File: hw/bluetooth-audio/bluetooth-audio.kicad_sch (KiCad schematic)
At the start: 1 part, among them U1 STM32WB55CGUx

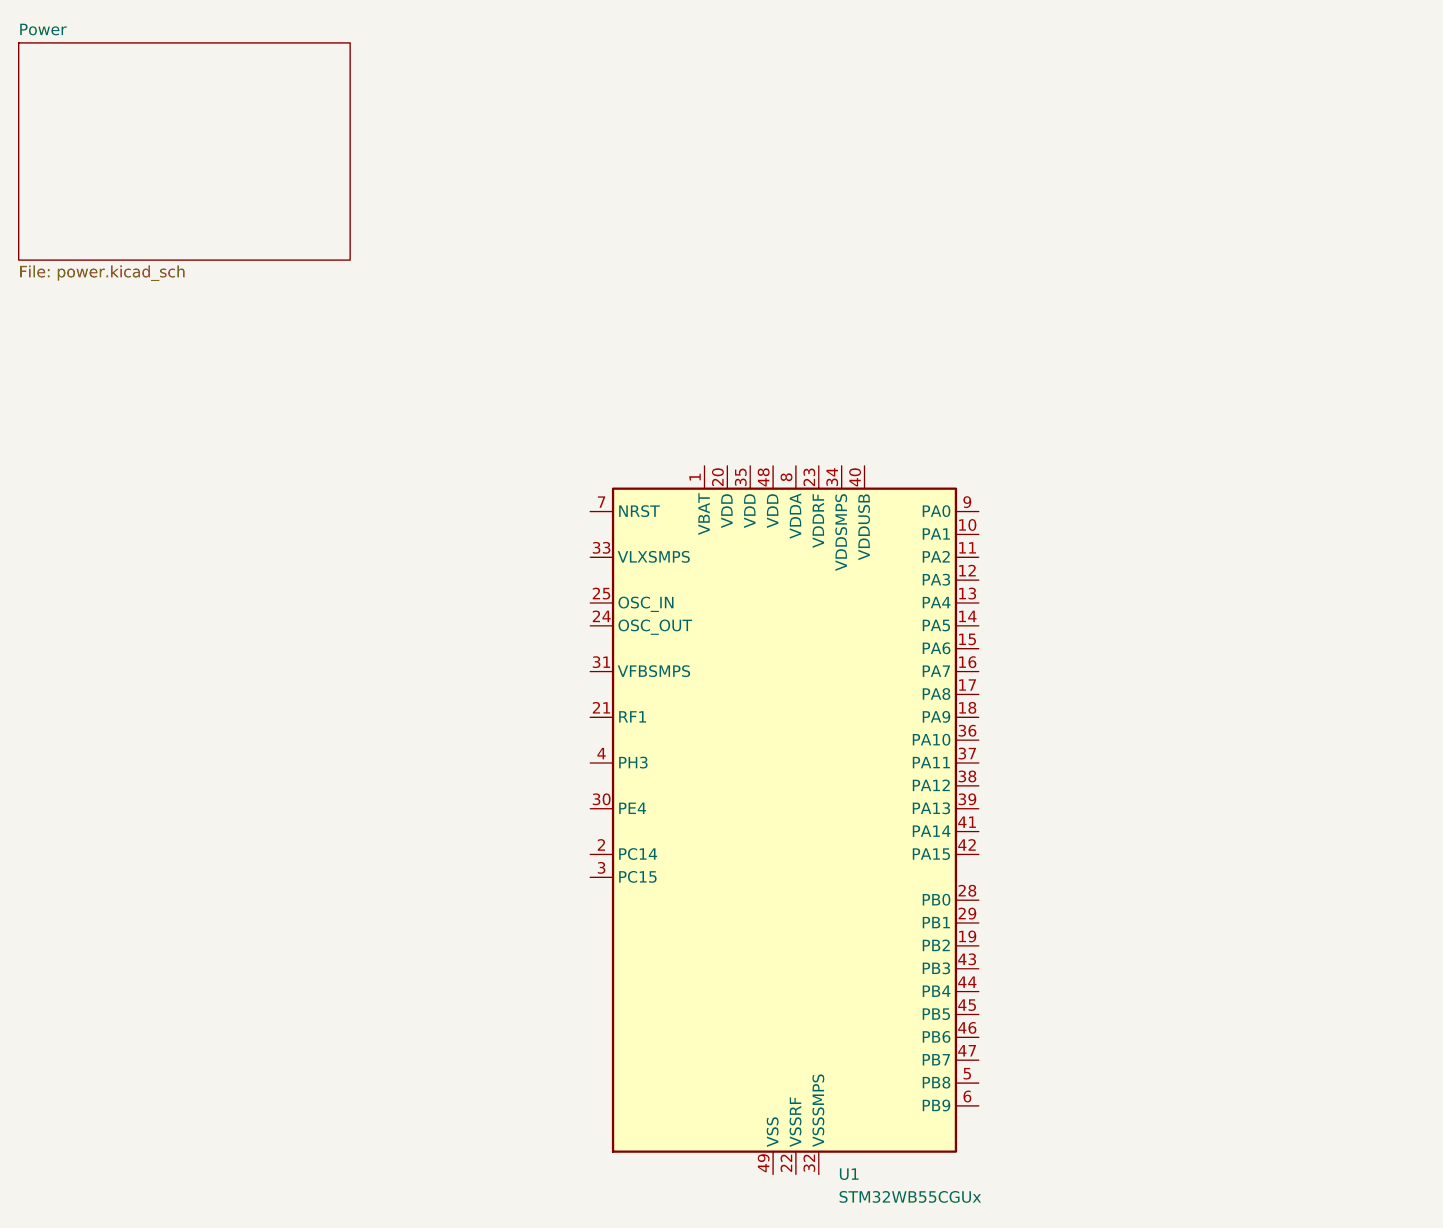
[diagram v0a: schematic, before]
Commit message: Microcontroller schematic sheet with decoupling, crystals, RF matching etc. Various app notes
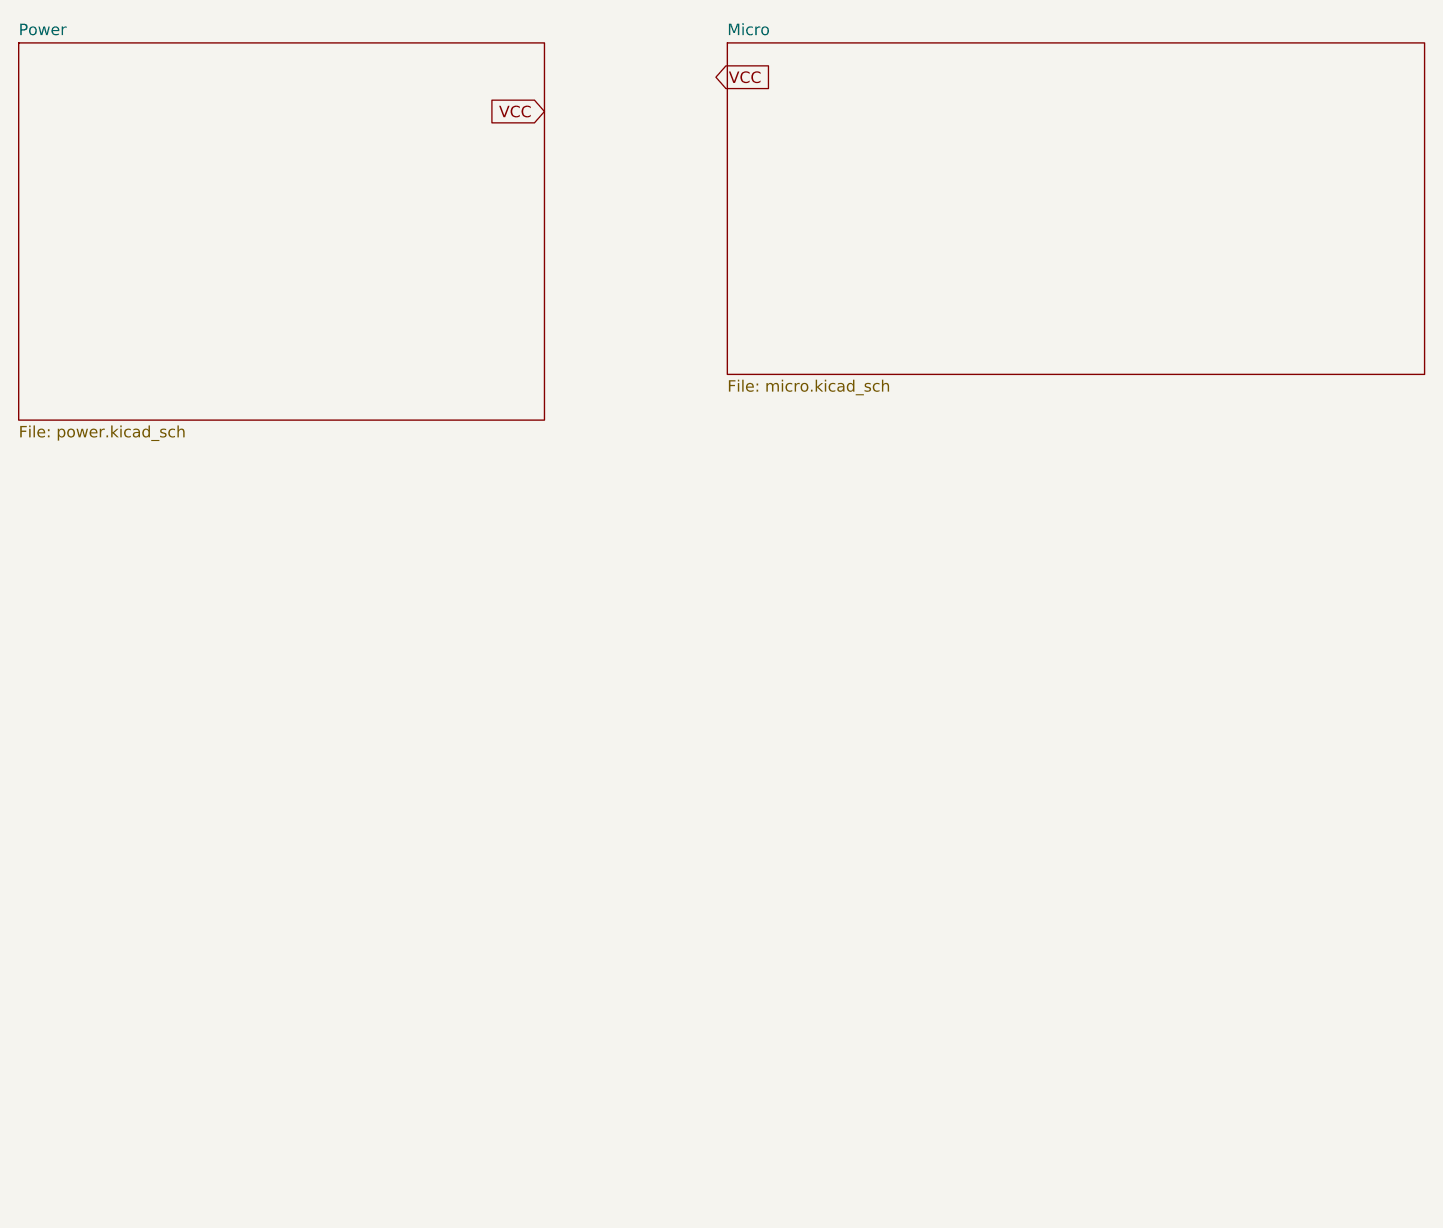
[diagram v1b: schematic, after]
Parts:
- removed U1: STM32WB55CGUx, Package_DFN_QFN:QFN-48-1EP_7x7mm_P0.5mm_EP5.6x5.6mm, symbol MCU_ST_STM32WB:STM32WB55CGUx
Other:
- added sheet Micro (micro.kicad_sch)
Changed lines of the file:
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@@
 (kicad_sch (version 20230121) (generator eeschema)
   (paper "A4")
-  (symbol (lib_id "MCU_ST_STM32WB:STM32WB55CGUx") (at 127 124.46 0) (unit 1)
-    (in_bom yes) (on_board yes) (dnp no) (fields_autoplaced)
-    (property "Reference" "U1" (at 134.2741 162.56 0)
-      (effects (font (size 1.27 1.27)) (justify left))
-    )
-    (property "Value" "STM32WB55CGUx" (at 134.2741 165.1 0)
-      (effects (font (size 1.27 1.27)) (justify left))
-    )
-    (property "Footprint" "Package_DFN_QFN:QFN-48-1EP_7x7mm_P0.5mm_EP5.6x5.6mm" (at 109.22 160.02 0)
+  (global_label "VCC" (shape input) (at 101.6 44.45 180) (fields_autoplaced)
+    (effects (font (size 1.27 1.27)) (justify right))
+    (property "Intersheetrefs" "${INTERSHEET_REFS}" (at 94.9862 44.45 0)
       (effects (font (size 1.27 1.27)) (justify right) hide)
     )
-    (property "Datasheet" "https://www.st.com/resource/en/datasheet/stm32wb55cg.pdf" (at 127 124.46 0)
-      (effects (font (size 1.27 1.27)) hide)
-    )
-    (property "Supplier Part Number" "C404023" (at 127 124.46 0)
-      (effects (font (size 1.27 1.27)) hide)
-    )
-    (pin "1")
-    (pin "10")
-    (pin "11")
-    (pin "12")
-    (pin "13")
-    (pin "14")
-    (pin "15")
-    (pin "16")
-    (pin "17")
-    (pin "18")
-    (pin "19")
-    (pin "2")
-    (pin "20")
-    (pin "21")
-    (pin "22")
-    (pin "23")
-    (pin "24")
-    (pin "25")
-    (pin "26")
-    (pin "27")
-    (pin "28")
-    (pin "29")
-    (pin "3")
-    (pin "30")
-    (pin "31")
-    (pin "32")
-    (pin "33")
-    (pin "34")
-    (pin "35")
-    (pin "36")
-    (pin "37")
-    (pin "38")
-    (pin "39")
-    (pin "4")
-    (pin "40")
-    (pin "41")
-    (pin "42")
-    (pin "43")
-    (pin "44")
-    (pin "45")
-    (pin "46")
-    (pin "47")
-    (pin "48")
-    (pin "49")
-    (pin "5")
-    (pin "6")
-    (pin "7")
-    (pin "8")
-    (pin "9")
-    (instances
-      (project "bluetooth-audio"
-        (path "/eafc8824-f117-40b2-99b0-597946d6c01d"
-          (reference "U1") (unit 1)
-        )
-      )
+  )
+  (global_label "VCC" (shape input) (at 120.65 40.64 0) (fields_autoplaced)
+    (effects (font (size 1.27 1.27)) (justify left))
+    (property "Intersheetrefs" "${INTERSHEET_REFS}" (at 127.2638 40.64 0)
+      (effects (font (size 1.27 1.27)) (justify left) hide)
     )
   )
-  (sheet (at 43.18 36.83) (size 36.83 24.13) (fields_autoplaced)
+  (sheet (at 43.18 36.83) (size 58.42 41.91) (fields_autoplaced)
     (stroke (width 0.1524) (type solid))
     (fill (color 0 0 0 0.0000))
@@
       (effects (font (size 1.27 1.27)) (justify left bottom))
     )
-    (property "Sheetfile" "power.kicad_sch" (at 43.18 61.5446 0)
+    (property "Sheetfile" "power.kicad_sch" (at 43.18 79.3246 0)
       (effects (font (size 1.27 1.27)) (justify left top))
     )
@@
       )
     )
+  )
+  (sheet (at 121.92 36.83) (size 77.47 36.83) (fields_autoplaced)
+    (stroke (width 0.1524) (type solid))
+    (fill (color 0 0 0 0.0000))
+    (property "Sheetname" "Micro" (at 121.92 36.1184 0)
+      (effects (font (size 1.27 1.27)) (justify left bottom))
+    )
+    (property "Sheetfile" "micro.kicad_sch" (at 121.92 74.2446 0)
+      (effects (font (size 1.27 1.27)) (justify left top))
+    )
+    (instances
+      (project "bluetooth-audio"
+        (path "/eafc8824-f117-40b2-99b0-597946d6c01d" (page "3"))
+      )
+    )

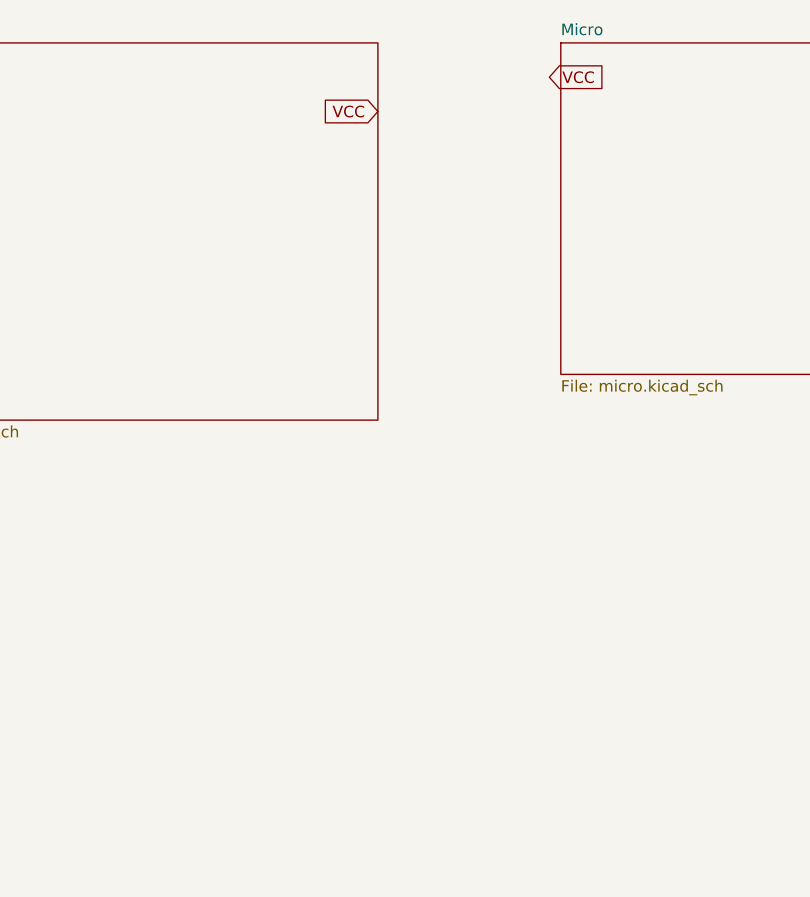
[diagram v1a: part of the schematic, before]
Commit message: Completed design with ESP32D0WD-v3, and JLC production files. High production cost due to req of PCBA standard, due to ESP32 pin pitch.
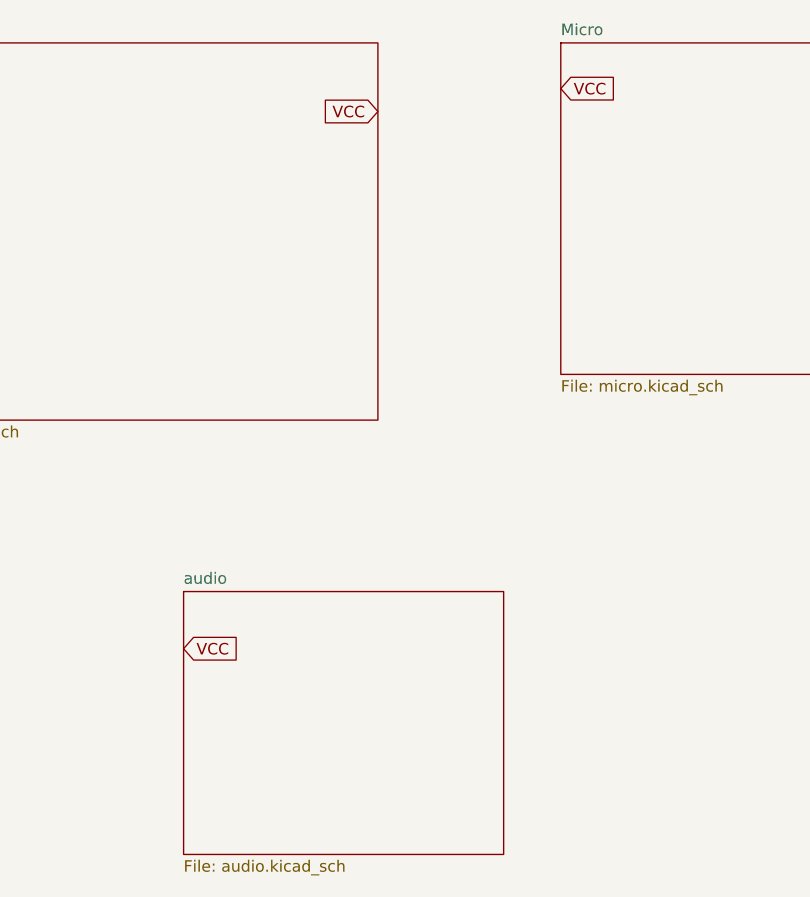
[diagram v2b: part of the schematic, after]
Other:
- added sheet audio (audio.kicad_sch)
